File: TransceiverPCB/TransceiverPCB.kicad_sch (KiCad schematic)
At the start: 227 parts, among them IC1 QPL6220QTR7, IC2 AD9218BSTZ-65, IC3 AD9763ASTZ, IC4 ADF4351BCPZ-RL7, J1 USB4085-GF-A_REVB, J2 RFPC-SMA27-F, J3 RFPC-SMA27-F, J4 FPGA JTAG, SW1 SW_Push, SW2 SW_Push, SW3 SW_Push, SW4 SW_Push, T1 ETC1-1-13TR, U1 XC7A35T-1FTG256C, U10 AP2112K-3.3TRG1, U11 LM66100DCKR, U12 ADL5387ACPZ-R7, U13 LP5912-1.0DRVR, U2 W25Q32JVSSIQ, U3 W25Q32JVSSIQ, U4 DSC1001CI2-100.0000T, U5 AP2112K-1.8TRG1, U6 ADL5375-05ACPZ-R7, U7 ADA4940-2ACPZ-R7, U8 ADL5320ARKZ-R7, U9 SC09147, X1 ABM8-272-T3

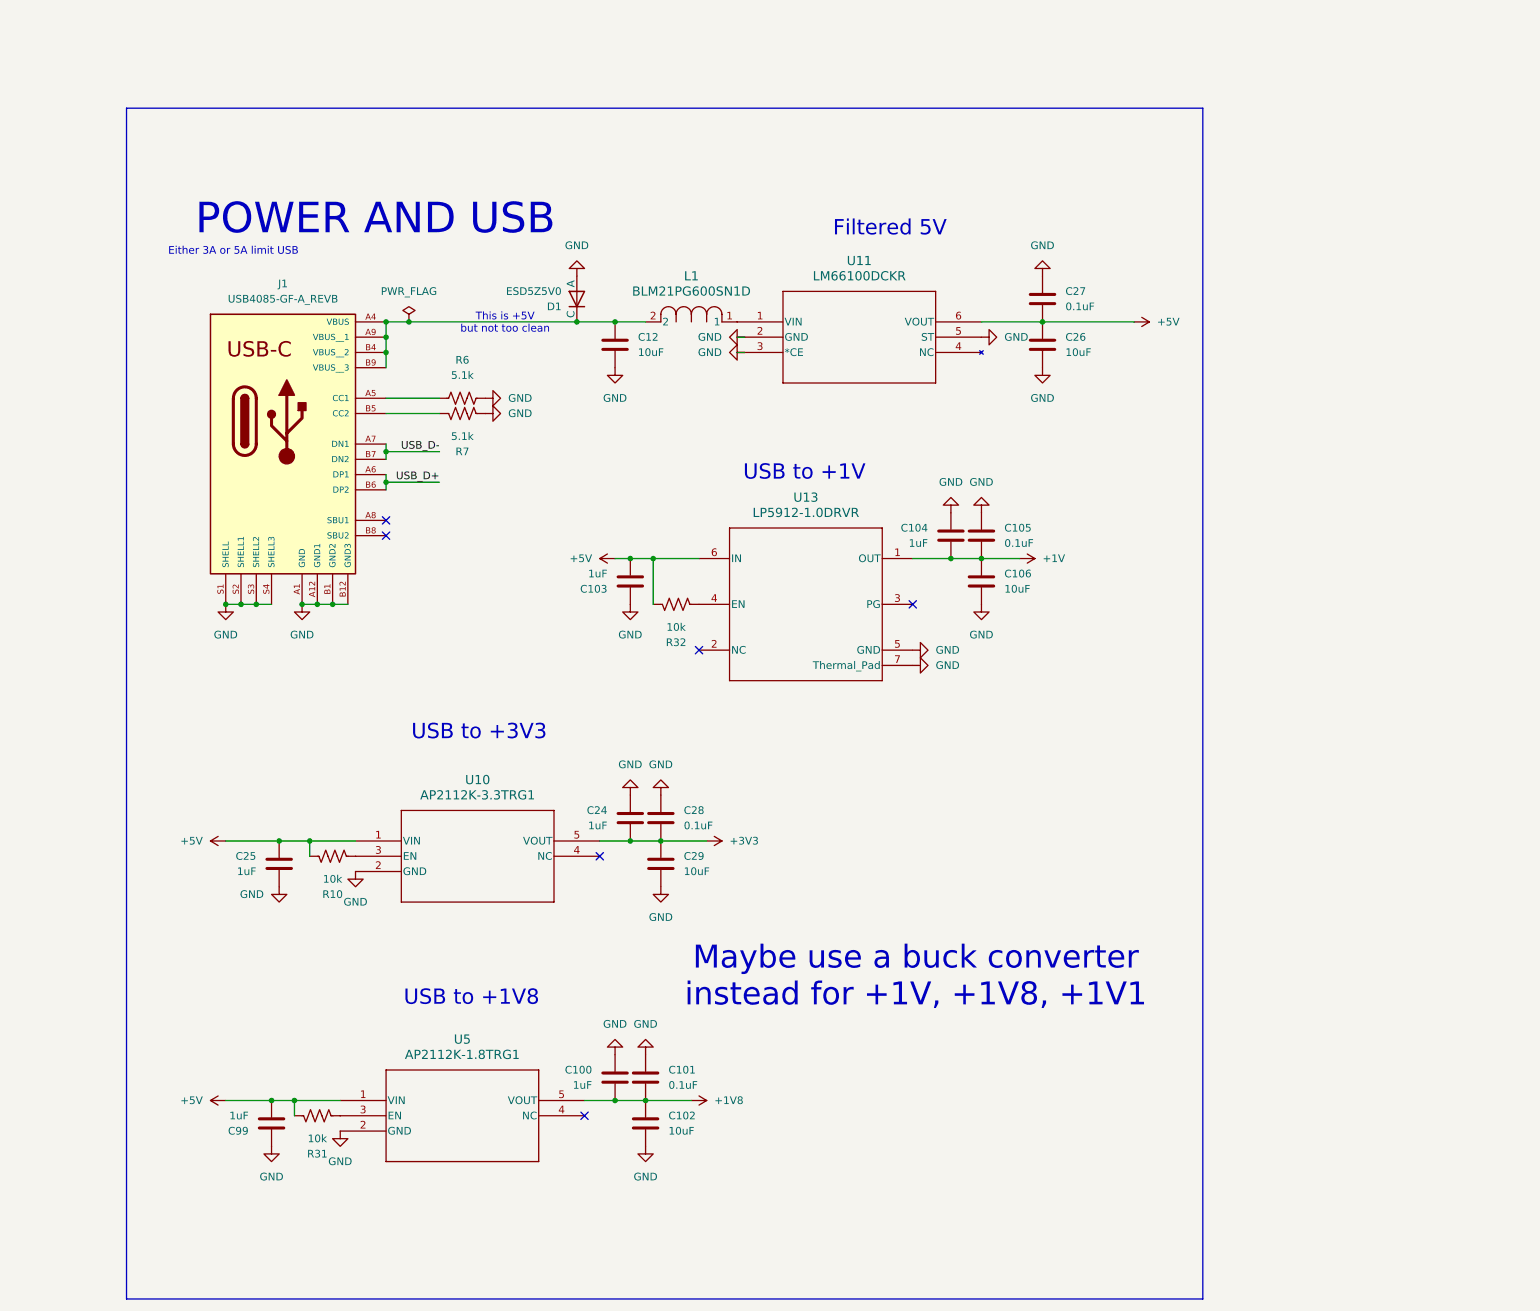
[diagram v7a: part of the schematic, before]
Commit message: Added +3V and LDO
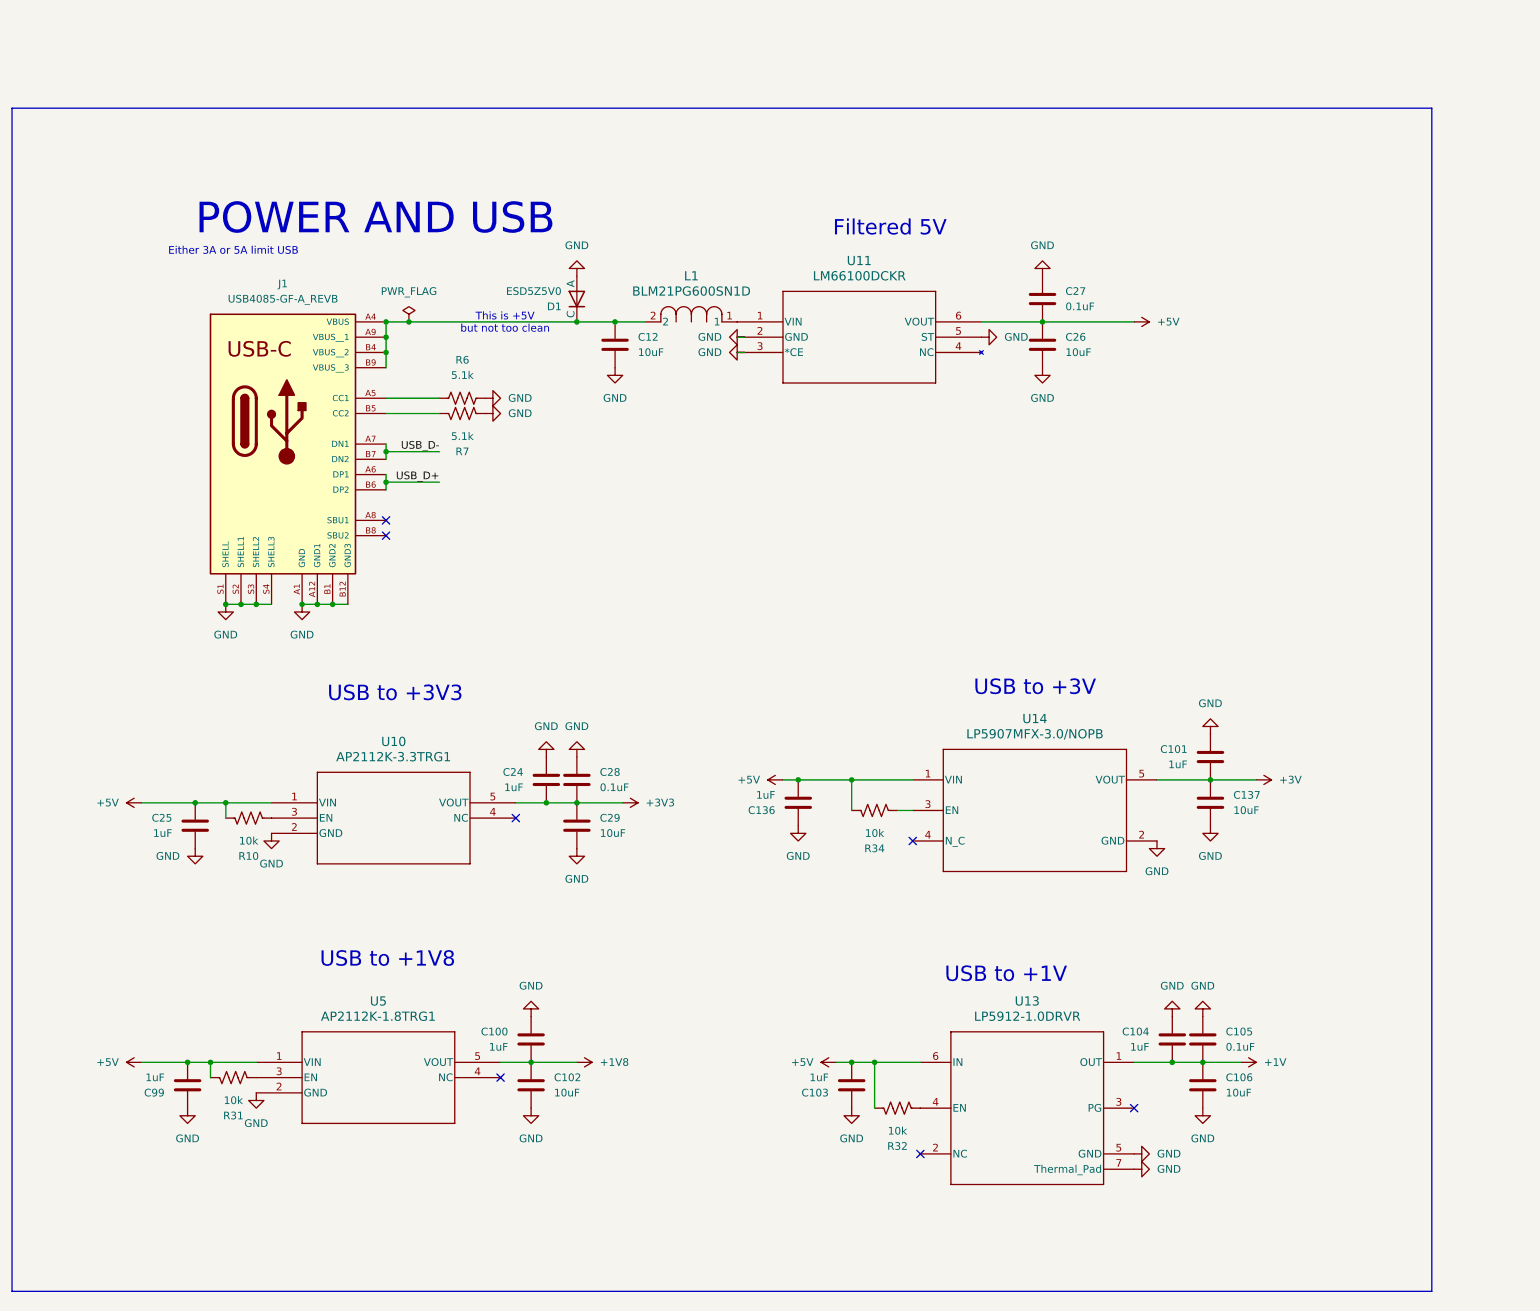
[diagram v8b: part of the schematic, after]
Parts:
- added C136: 1uF, symbol Device:C
- added C137: 10uF, symbol Device:C
- added R34: 10k, symbol Device:R_US
- added U14: LP5907MFX-3.0/NOPB, DBV0005A_N, symbol LIB_IRISHSAT:LP5907MFX-3.0_NOPB
- C101: value 0.1uF -> 1uF
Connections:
- net +1V8: no longer C101.2
- net +3V: now also C101.2, C137.2, U14.5 (VOUT)
- net +5V: now also C136.2, R34.1, U14.1 (VIN)
- net GND: now also C136.1, C137.1, U14.2 (GND)
- new net: R34.2, U14.3 (EN)
- no-connect marks 44 -> 45
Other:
- note added: "USB to +3V"
- note removed: "Maybe use a buck converter instead for +1V, +1V8, +1V1"
- moved on the sheet: C100, C102, C103, C104, C105, C106, C24, C25, C28, C29, C99, R10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
